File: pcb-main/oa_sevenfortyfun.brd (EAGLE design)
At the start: 88.9 x 71.1 mm, 46 parts, among them J1 1X01-TERM, J2 1X01-TERM, J3 1X01-TERM, J4 1X01-TERM, J5 1X01-TERM, J6 1X01-TERM, J7 1X01-TERM, J8 1X01-TERM, J9 2X04SHR, Q1 2N3904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

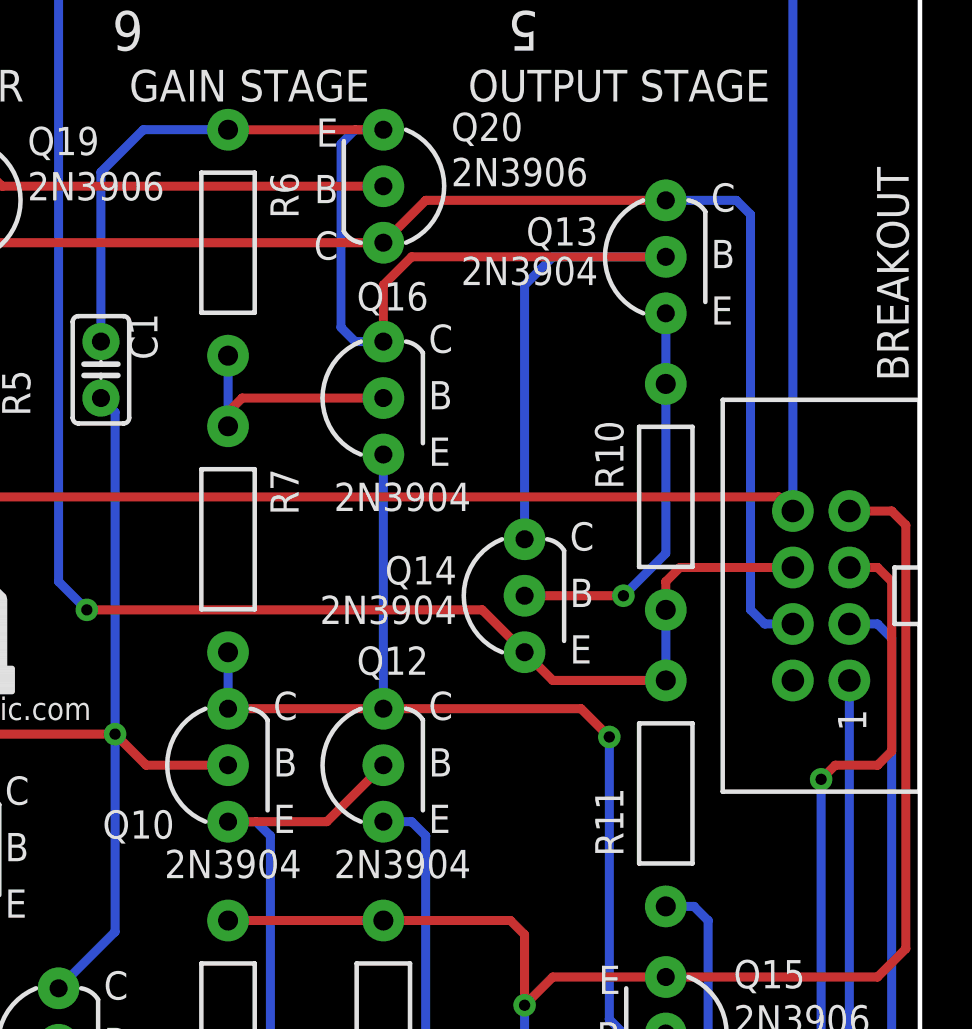
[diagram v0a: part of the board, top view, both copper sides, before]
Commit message: added breakout board
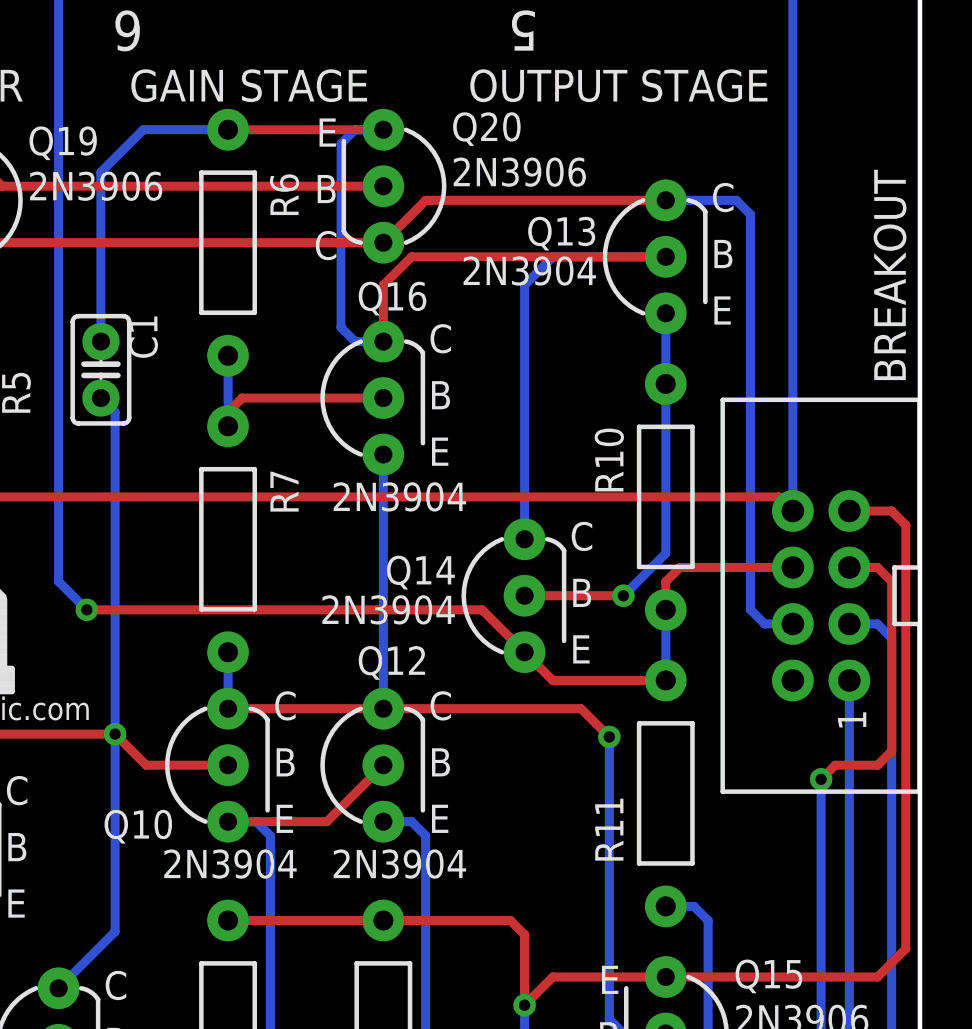
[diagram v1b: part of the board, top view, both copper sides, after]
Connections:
- net IN+ renamed NON-INVERTING(+)
- net IN- renamed INVERTING(-)
- net OFFSET_N1 renamed OFFSET_NULL1
- net OFFSET_N2 renamed OFFSET_NULL2
- net OUT renamed OUTPUT
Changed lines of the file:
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@@
 <setting verticaltext="up"/>
 </settings>
-<grid distance="10" unitdist="mil" unit="mil" style="lines" multiple="1" display="yes" altdistance="0.025" altunitdist="inch" altunit="inch"/>
+<grid distance="25" unitdist="mil" unit="mil" style="lines" multiple="1" display="yes" altdistance="0.025" altunitdist="inch" altunit="inch"/>
 <layers>
 <layer number="1" name="Top" color="4" fill="1" visible="yes" active="yes"/>
@@
 <text x="68.58" y="57.785" size="1.4224" layer="21" font="vector" ratio="15">OUTPUT STAGE</text>
 <wire x1="0" y1="40.005" x2="0" y2="31.115" width="0.2032" layer="20" curve="-180"/>
-<text x="88.392" y="45.212" size="1.4224" layer="21" font="vector" ratio="15" rot="R90">BREAKOUT</text>
+<text x="88.265" y="45.085" size="1.4224" layer="21" font="vector" ratio="15" rot="R90">BREAKOUT</text>
 <text x="8.89" y="0.635" size="1.5748" layer="21" font="vector" ratio="15">OFFSET NULL</text>
 <text x="17.145" y="9.271" size="1.778" layer="21" font="vector" ratio="15">1</text>
@@
 <element name="Q10" library="Ai_DiscreteSemis" package="TO-92-NPN" value="2N3904" x="57.785" y="27.94" smashed="yes">
 <attribute name="NAME" x="55.372" y="25.908" size="1.27" layer="25" font="vector" ratio="15" rot="R180"/>
-<attribute name="VALUE" x="61.087" y="24.13" size="1.27" layer="25" font="vector" ratio="15" rot="R180"/>
+<attribute name="VALUE" x="60.96" y="24.13" size="1.27" layer="25" font="vector" ratio="15" rot="R180"/>
 </element>
 <element name="Q11" library="Ai_DiscreteSemis" package="TO-92-NPN" value="2N3904" x="50.165" y="15.367"/>
@@
 <element name="Q12" library="Ai_DiscreteSemis" package="TO-92-NPN" value="2N3904" x="64.77" y="27.94" smashed="yes">
 <attribute name="NAME" x="66.802" y="33.274" size="1.27" layer="25" font="vector" ratio="15" rot="R180"/>
-<attribute name="VALUE" x="68.707" y="24.13" size="1.27" layer="25" font="vector" ratio="15" rot="R180"/>
+<attribute name="VALUE" x="68.58" y="24.13" size="1.27" layer="25" font="vector" ratio="15" rot="R180"/>
 </element>
 <element name="Q16" library="Ai_DiscreteSemis" package="TO-92-NPN" value="2N3904" x="64.77" y="44.45" smashed="yes">
 <attribute name="NAME" x="66.802" y="49.657" size="1.27" layer="25" font="vector" ratio="15" rot="R180"/>
-<attribute name="VALUE" x="68.707" y="40.64" size="1.27" layer="25" font="vector" ratio="15" rot="R180"/>
+<attribute name="VALUE" x="68.58" y="40.64" size="1.27" layer="25" font="vector" ratio="15" rot="R180"/>
 </element>
 <element name="Q13" library="Ai_DiscreteSemis" package="TO-92-NPN" value="2N3904" x="77.47" y="50.8"/>
 <element name="Q14" library="Ai_DiscreteSemis" package="TO-92-NPN" value="2N3904" x="71.12" y="35.56"/>
 <element name="R10" library="Ai_Passives" package="RES-AXIAL-0.4" value="25" x="77.47" y="40.005" smashed="yes" rot="R270">
-<attribute name="NAME" x="74.295" y="43.434" size="1.27" layer="25" font="vector" ratio="15" rot="R270"/>
+<attribute name="NAME" x="74.295" y="43.18" size="1.27" layer="25" font="vector" ratio="15" rot="R270"/>
 </element>
 <element name="R11" library="Ai_Passives" package="RES-AXIAL-0.4" value="50" x="77.47" y="26.67" smashed="yes" rot="R270">
-<attribute name="NAME" x="74.295" y="26.924" size="1.27" layer="25" font="vector" ratio="15" rot="R270"/>
+<attribute name="NAME" x="75.565" y="23.495" size="1.27" layer="25" font="vector" ratio="15" rot="R90"/>
 </element>
 <element name="Q15" library="Ai_DiscreteSemis" package="TO-92-PNP" value="2N3906" x="77.47" y="15.875"/>
@@
 <wire x1="21.59" y1="26.797" x2="20.32" y2="28.067" width="0.4064" layer="1"/>
 </signal>
-<signal name="OFFSET_N2">
+<signal name="OFFSET_NULL2">
 <contactref element="Q7" pad="1"/>
 <contactref element="R2" pad="P$1"/>
@@
 <wire x1="12.7" y1="36.83" x2="27.94" y2="36.83" width="0.4064" layer="1"/>
 </signal>
-<signal name="IN+">
+<signal name="NON-INVERTING(+)">
 <contactref element="Q2" pad="2"/>
 <contactref element="J3" pad="1"/>
@@
 <via x="84.455" y="27.305" extent="1-16" drill="0.508"/>
 </signal>
-<signal name="IN-">
+<signal name="INVERTING(-)">
 <contactref element="Q1" pad="2"/>
 <contactref element="J2" pad="1"/>
@@
 <wire x1="77.47" y1="37.465" x2="77.47" y2="45.085" width="0.4064" layer="16"/>
 </signal>
-<signal name="OUT">
+<signal name="OUTPUT">
 <contactref element="J6" pad="1"/>
 <contactref element="J9" pad="6"/>
@@
 <wire x1="80.645" y1="53.34" x2="77.47" y2="53.34" width="0.4064" layer="16"/>
 </signal>
-<signal name="OFFSET_N1">
+<signal name="OFFSET_NULL1">
 <contactref element="J1" pad="1"/>
 <contactref element="Q6" pad="1"/>
